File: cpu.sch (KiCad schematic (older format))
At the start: 3 parts

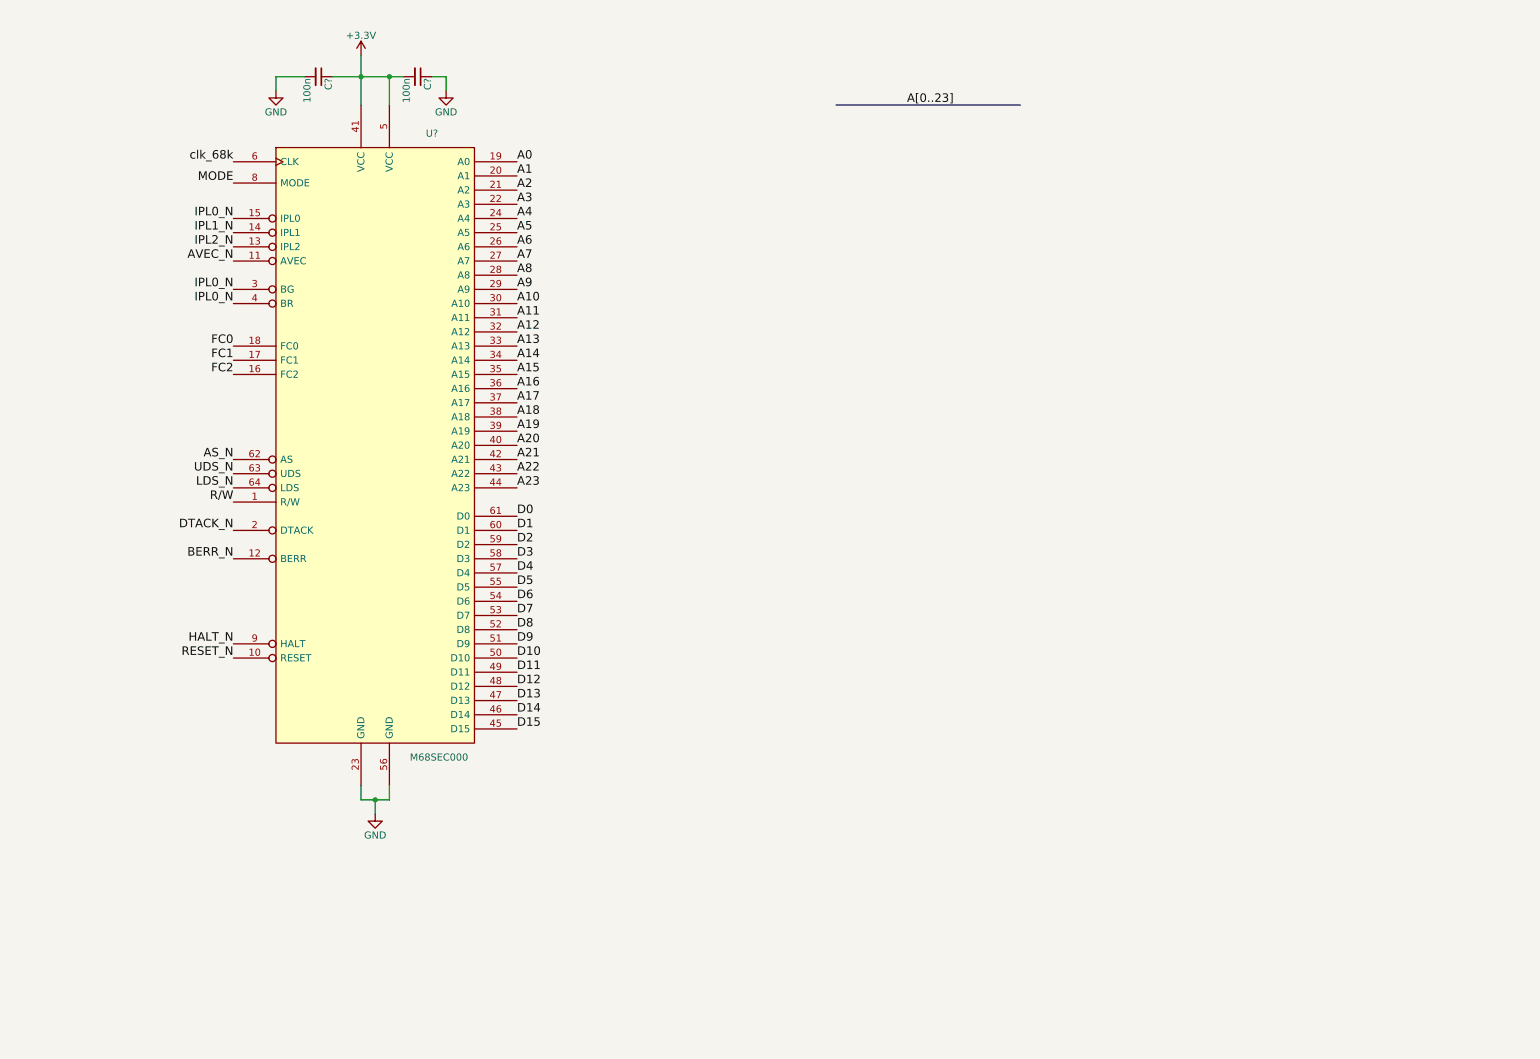
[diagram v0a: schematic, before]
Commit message: added sram symbol
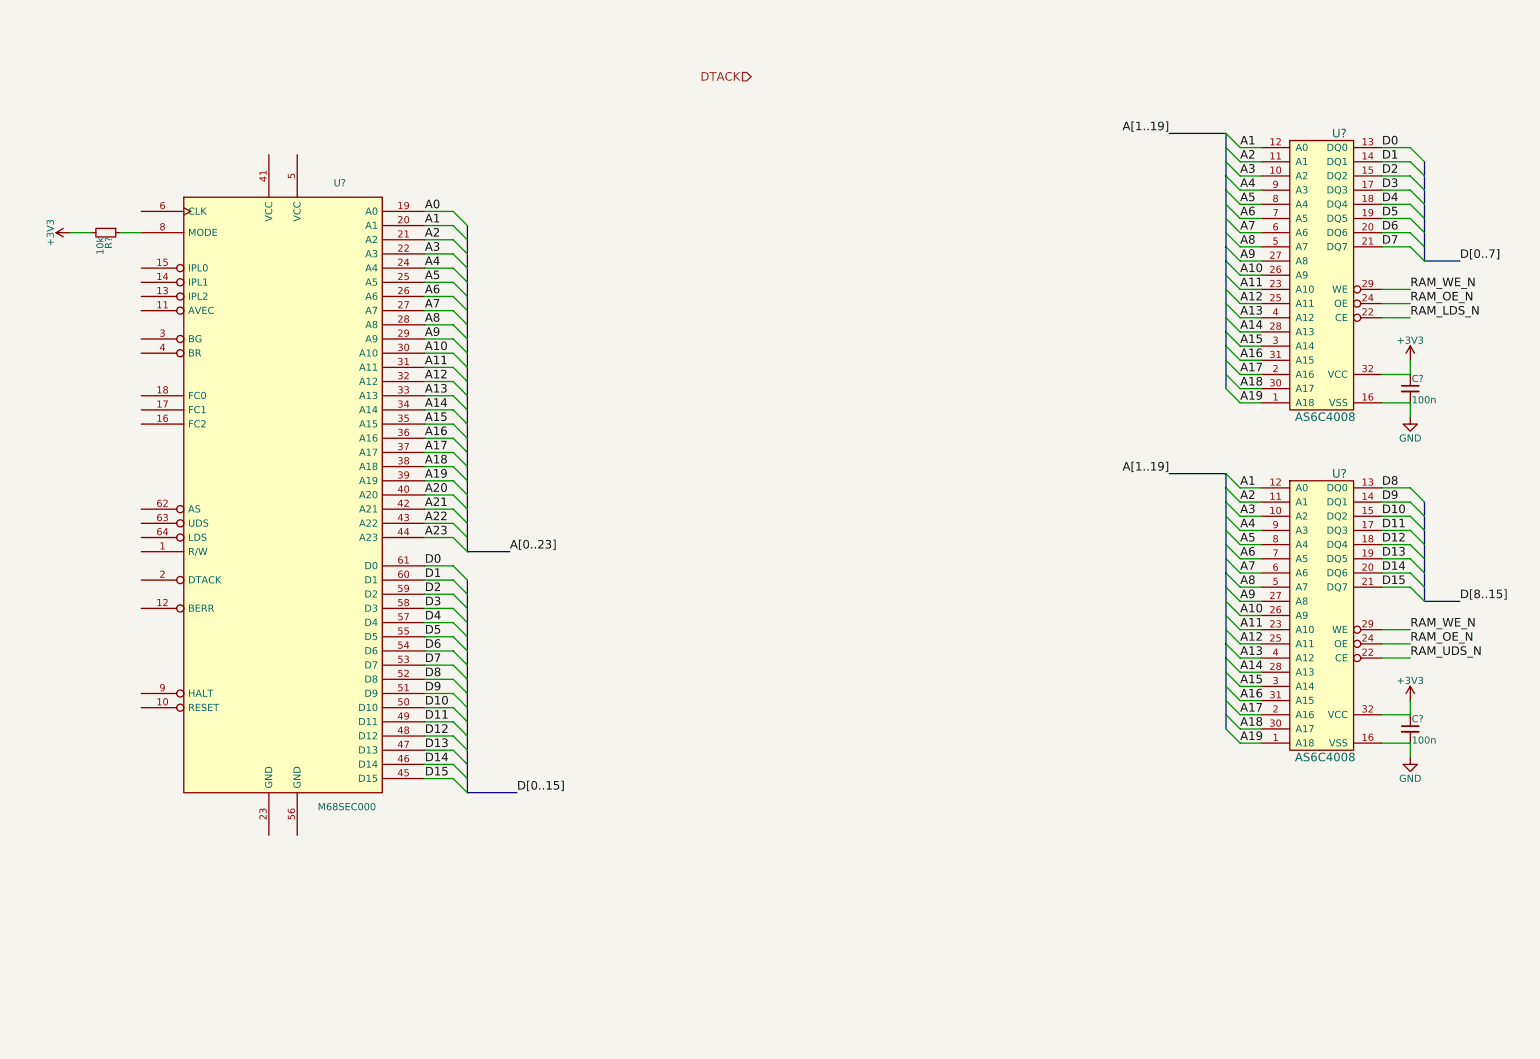
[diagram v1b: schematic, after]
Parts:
- removed C? (x2): 100n, symbol C_Small
- removed U?: M68SEC000, symbol M68SEC000
- added C? (x2): 100n, symbol C_Small
- added R?: 10k, symbol R_Small
- added U? (x2): AS6C4008, symbol AS6C4008
- added U?: M68SEC000, symbol M68SEC000
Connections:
- net +3V3: now also C?.1, C?.1, R?.2, U?.32 (VCC), U?.32 (VCC)
- net A0: now also U?.19 (A0)
- net A1: now also U?.12 (A0), U?.12 (A0), U?.20 (A1)
- net A10: now also U?.26 (A9), U?.26 (A9), U?.30 (A10)
- net A11: now also U?.23 (A10), U?.23 (A10), U?.31 (A11)
- net A12: now also U?.25 (A11), U?.25 (A11), U?.32 (A12)
- net A13: now also U?.33 (A13), U?.4 (A12), U?.4 (A12)
- net A14: now also U?.28 (A13), U?.28 (A13), U?.34 (A14)
- net A15: now also U?.3 (A14), U?.3 (A14), U?.35 (A15)
- net A16: now also U?.31 (A15), U?.31 (A15), U?.36 (A16)
- net A17: now also U?.2 (A16), U?.2 (A16), U?.37 (A17)
- net A18: now also U?.30 (A17), U?.30 (A17), U?.38 (A18)
- net A19: now also U?.1 (A18), U?.1 (A18), U?.39 (A19)
- net A2: now also U?.11 (A1), U?.11 (A1), U?.21 (A2)
- net A20: now also U?.40 (A20)
- net A21: now also U?.42 (A21)
- net A22: now also U?.43 (A22)
- net A23: now also U?.44 (A23)
- net A3: now also U?.10 (A2), U?.10 (A2), U?.22 (A3)
- net A4: now also U?.24 (A4), U?.9 (A3), U?.9 (A3)
- net A5: now also U?.25 (A5), U?.8 (A4), U?.8 (A4)
- net A6: now also U?.26 (A6), U?.7 (A5), U?.7 (A5)
- net A7: now also U?.27 (A7), U?.6 (A6), U?.6 (A6)
- net A8: now also U?.28 (A8), U?.5 (A7), U?.5 (A7)
- net A9: now also U?.27 (A8), U?.27 (A8), U?.29 (A9)
- net D0: now also U?.13 (DQ0), U?.61 (D0)
- net D1: now also U?.14 (DQ1), U?.60 (D1)
- net D10: now also U?.15 (DQ2), U?.50 (D10)
- net D11: now also U?.17 (DQ3), U?.49 (D11)
- net D12: now also U?.18 (DQ4), U?.48 (D12)
- net D13: now also U?.19 (DQ5), U?.47 (D13)
- net D14: now also U?.20 (DQ6), U?.46 (D14)
- net D15: now also U?.21 (DQ7), U?.45 (D15)
- net D2: now also U?.15 (DQ2), U?.59 (D2)
- net D3: now also U?.17 (DQ3), U?.58 (D3)
- net D4: now also U?.18 (DQ4), U?.57 (D4)
- net D5: now also U?.19 (DQ5), U?.55 (D5)
- net D6: now also U?.20 (DQ6), U?.54 (D6)
- net D7: now also U?.21 (DQ7), U?.53 (D7)
- net D8: now also U?.13 (DQ0), U?.52 (D8)
- net D9: now also U?.14 (DQ1), U?.51 (D9)
- net GND: now also C?.2, C?.2, U?.16 (VSS), U?.16 (VSS)
- new net: R?.1, U?.8 (MODE)
- new net RAM_LDS_N: U?.22 (CE)
- new net RAM_OE_N: U?.24 (OE), U?.24 (OE)
- new net RAM_UDS_N: U?.22 (CE)
- new net RAM_WE_N: U?.29 (WE), U?.29 (WE)

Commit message: boot process
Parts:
- added C? (x7): 100n, symbol C_Small
- added J?: JTAG, symbol CONN_01X06
- added J?: ISP, symbol CONN_02X03
- added R?: 1k, symbol R_Small
- added R? (x10): 10k, symbol R_Small
- added U?: XC9572XL-VQ44, symbol XC9572XL-VQ44
- added U?: ATMEGA328P-AU, TQFP32, symbol ATMEGA328P-AU
- added U?: 25LC_EEPROM, symbol 25LC_EEPROM
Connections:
- net +3V3: now also U?.41 (VCC), U?.5 (VCC), C?.2, C?.2, C?.2, C?.2, J?.1 (P1), J?.2 (P2), R?.1, R?.1, R?.1, R?.1, R?.1, R?.1, R?.1, R?.1, R?.1, R?.1, U?.3 (~WP), U?.4 (VCC), U?.6 (VCC), U?.7 (~HOLD), U?.8 (Vcc)
- net A20: now also U?.39 (P39)
- net A21: now also U?.40 (P40)
- net A22: now also U?.41 (P41)
- net A23: now also U?.42 (P42)
- net D0: now also U?.2 (P2)
- net D1: now also U?.3 (P3)
- net D10: now also U?.18 (P18)
- net D11: now also U?.19 (P19)
- net D12: now also U?.20 (P20)
- net D13: now also U?.21 (P21)
- net D14: now also U?.22 (P22)
- net D15: now also U?.23 (P23)
- net D2: now also U?.5 (P5)
- net D3: now also U?.6 (P6)
- net D4: now also U?.7 (P7)
- net D5: now also U?.8 (P8)
- net D6: now also U?.12 (P12)
- net D7: now also U?.13 (P13)
- net D8: now also U?.14 (P14)
- net D9: now also U?.16 (P16)
- net GND: now also C?.1, C?.1, C?.1, C?.1, C?.1, C?.1, C?.1, J?.2 (P2), J?.6 (P6), U?.17 (GND), U?.21 (GND), U?.25 (GND), U?.3 (GND), U?.4 (GND), U?.4 (GND), U?.5 (GND)
- net RAM_LDS_N: now also U?.32 (P32)
- net RAM_UDS_N: now also U?.37 (P37)
- net at U?.1 (R/W): now also R?.1
- net RESET_N: now reaches U?.10 (RESET)
- net RESET_N: now also R?.2, U?.23 ((PCINT8/ADC0)PC0)
- net AVEC_N: now reaches U?.11 (AVEC)
- net AVEC_N: now also R?.2
- net BERR_N: now reaches U?.12 (BERR)
- net BERR_N: now also R?.2
- net IPL2_N: now reaches U?.13 (IPL2)
- net IPL2_N: now also R?.2
- net IPL1_N: now reaches U?.14 (IPL1)
- net IPL1_N: now also R?.2
- net IPL0_N: now reaches U?.15 (IPL0)
- net IPL0_N: now also R?.2
- net FC2: now reaches U?.16 (FC2)
- net FC1: now reaches U?.17 (FC1)
- net FC0: now reaches U?.18 (FC0)
- net DTACK_N: now reaches U?.2 (DTACK)
- net DTACK_N: now also R?.2, U?.27 ((PCINT12/SDA/ADC4)PC4)
- net BG_N: now reaches U?.3 (BG)
- net BG_N: now also R?.2
- net BR_N: now reaches U?.4 (BR)
- net BR_N: now also R?.2
- net CLK_68k: now reaches U?.6 (CLK)
- net AS_N: now reaches U?.62 (AS)
- net UDS_N: now reaches U?.63 (UDS)
- net UDS_N: now also U?.25 ((PCINT10/ADC2)PC2), U?.30 (P30)
- net LDS_N: now reaches U?.64 (LDS)
- net LDS_N: now also U?.26 ((PCINT11/ADC3)PC3), U?.29 (P29)
- net HALT_N: now reaches U?.9 (HALT)
- net HALT_N: now also R?.2, U?.24 ((PCINT9/ADC1)PC1)
- net RAM_OE_N renamed OE_N
- net OE_N: now also U?.28 (P28)
- net RAM_WE_N renamed R/W
- net R/W: now also R?.2, U?.12 ((PCINT0/CLKO/ICP1)PB0), U?.27 (P27)
- new net: C?.2, U?.15 (VCCINT)
- new net: C?.2, U?.26 (VCCIO)
- new net: C?.2, U?.35 (VCCINT)
- new net BOOT: U?.13 ((PCINT1/OC1A)PB1), U?.36 (GTS1)
- new net CLK_CPLD: U?.43 (GCK1)
- new net CS_EE_N: U?.1 (~CS), U?.14 ((PCINT2/OC1B/~SS~)PB2)
- new net DCLK: U?.44 (GCK2), U?.7 ((PCINT6/XTAL1/TOSC1)PB6)
- new net DIN: U?.31 (P31), U?.8 ((PCINT7/XTAL2/TOSC2)PB7)
- new net EXT_CS_N: U?.38 (P38)
- new net MISO: J?.1 (P1), U?.16 ((PCINT4/MISO)PB4), U?.2 (MISO)
- new net MOSI: J?.4 (P4), U?.15 ((PCINT3/OC2A/MOSI)PB3), U?.5 (MOSI)
- new net RESET_AVR_N: J?.5 (P5), U?.29 ((PCINT14/~RESET~)PC6)
- new net RX: U?.30 ((PCINT16/RXD)PD0)
- new net SCK: J?.3 (P3), U?.17 ((PCINT5/SCK)PB5), U?.6 (SCK)
- new net TCK: J?.3 (P3), U?.11 (TCK)
- new net TDI: J?.5 (P5), U?.9 (TDI)
- new net TDO: J?.4 (P4), U?.24 (TDO)
- new net TMS: J?.6 (P6), U?.10 (TMS)
- new net TX: U?.31 ((PCINT17/TXD)PD1)
